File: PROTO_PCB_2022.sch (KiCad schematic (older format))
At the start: 38 parts, among them J1 12V_BATT, J10 12V_OUT_AUX, J11 SW_START, J12 VESC_START, J13 5V_OUT_AUX, J2 SW_KILL_DRIVER, J3 SW_KILL_LEFT, J4 SW_KILL_RIGHT, J5 ECU_POWER, J6 SW_BRAKE, J7 12V_OUT_HORN, J8 BRAKELIGHT_POWER, J9 12V_OUT_TEL, Q1 MOSFET_ECU, Q2 MOSFET_BRAKE_LIGHT, U1 LD1117S50TR_SOT223

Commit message: did some more layout work
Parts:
- removed F6, F7: 1A, Fuse:Fuseholder_Blade_Mini_Keystone_3568, symbol Device:Fuse
- removed J10: 12V_OUT_AUX, Connector_Molex:Molex_Micro-Fit_3.0_43650-0200_1x02_P3.00mm_Horizontal, symbol PROTO_PCB_2022-rescue:B2B-PH-K-S_LF__SN_-dk_Rectangular-Connectors-Headers-Male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
- removed J13: 5V_OUT_AUX, Connector_Molex:Molex_Micro-Fit_3.0_43650-0200_1x02_P3.00mm_Horizontal, symbol PROTO_PCB_2022-rescue:B2B-PH-K-S_LF__SN_-dk_Rectangular-Connectors-Headers-Male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
- J9: value 12V_OUT_TEL -> 12V_OUT_AUX
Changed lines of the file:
@@
 P 6200 1500
 F 0 "J9" V 6291 1372 50  0000 R CNN
-F 1 "12V_OUT_TEL" V 6200 1372 50  0000 R CNN
+F 1 "12V_OUT_AUX" V 6200 1372 50  0000 R CNN
 F 2 "Connector_Molex:Molex_Micro-Fit_3.0_43650-0200_1x02_P3.00mm_Horizontal" H 6400 1700 60  0001 L CNN
 F 3 "" H 6400 1800 60  0001 L CNN
@@
 	1    0    0    -1
 $EndComp
-$Comp
-L Device:Fuse F5
-U 1 1 62844314
-P 5800 1400
-F 0 "F5" V 5603 1400 50  0000 C CNN
-F 1 "1A" V 5694 1400 50  0000 C CNN
-F 2 "Fuse:Fuseholder_Blade_Mini_Keystone_3568" V 5730 1400 50  0001 C CNN
-F 3 "https://www.digikey.ca/en/products/detail/littelfuse-inc/178-6164-0001/2515818" H 5800 1400 50  0001 C CNN
-	1    5800 1400
-	0    1    1    0
-$EndComp
 Wire Wire Line
 	5500 1150 5500 1400
-Wire Wire Line
-	5500 1400 5650 1400
-Wire Wire Line
-	5950 1400 6100 1400
 $Comp
 L power:GND #PWR012
@@
 Wire Wire Line
 	5500 1500 5500 1700
-$Comp
-L PROTO_PCB_2022-rescue:B2B-PH-K-S_LF__SN_-dk_Rectangular-Connectors-Headers-Male-Pins-Proto-PCB's-combined-rescue-Proto-PCB's-combined-rescue J10
-U 1 1 6284D1CD
-P 7700 1500
-F 0 "J10" V 7791 1372 50  0000 R CNN
-F 1 "12V_OUT_AUX" V 7700 1372 50  0000 R CNN
-F 2 "Connector_Molex:Molex_Micro-Fit_3.0_43650-0200_1x02_P3.00mm_Horizontal" H 7900 1700 60  0001 L CNN
-F 3 "" H 7900 1800 60  0001 L CNN
-F 4 "" H 7900 1900 60  0001 L CNN "DigiKeyPN"
-F 5 "0436500201" H 7900 2000 60  0001 L CNN "MPN"
-	1    7700 1500
-	0    -1   -1   0
-$EndComp
-$Comp
-L power:+12V #PWR015
-U 1 1 6284D1D7
-P 7000 1150
-F 0 "#PWR015" H 7000 1000 50  0001 C CNN
-F 1 "+12V" H 7015 1323 50  0000 C CNN
-F 2 "" H 7000 1150 50  0001 C CNN
-F 3 "" H 7000 1150 50  0001 C CNN
-	1    7000 1150
-	1    0    0    -1
-$EndComp
-$Comp
-L Device:Fuse F6
-U 1 1 6284D1E1
-P 7300 1400
-F 0 "F6" V 7103 1400 50  0000 C CNN
-F 1 "1A" V 7194 1400 50  0000 C CNN
-F 2 "Fuse:Fuseholder_Blade_Mini_Keystone_3568" V 7230 1400 50  0001 C CNN
-F 3 "https://www.digikey.ca/en/products/detail/littelfuse-inc/178-6164-0001/2515818" H 7300 1400 50  0001 C CNN
-	1    7300 1400
-	0    1    1    0
-$EndComp
-Wire Wire Line
-	7000 1150 7000 1400
-Wire Wire Line
-	7000 1400 7150 1400
-Wire Wire Line
-	7450 1400 7600 1400
-$Comp
-L power:GND #PWR016
-U 1 1 6284D1EE
-P 7000 1700
-F 0 "#PWR016" H 7000 1450 50  0001 C CNN
-F 1 "GND" H 7005 1527 50  0000 C CNN
-F 2 "" H 7000 1700 50  0001 C CNN
-F 3 "" H 7000 1700 50  0001 C CNN
-	1    7000 1700
-	1    0    0    -1
-$EndComp
-Wire Wire Line
-	7600 1500 7000 1500
-Wire Wire Line
-	7000 1500 7000 1700
 $Comp
 L PROTO_PCB_2022-rescue:B2B-PH-K-S_LF__SN_-dk_Rectangular-Connectors-Headers-Male-Pins-Proto-PCB's-combined-rescue-Proto-PCB's-combined-rescue J2
@@
 Wire Wire Line
 	2650 3500 2650 3750
-$Comp
-L PROTO_PCB_2022-rescue:B2B-PH-K-S_LF__SN_-dk_Rectangular-Connectors-Headers-Male-Pins-Proto-PCB's-combined-rescue-Proto-PCB's-combined-rescue J13
-U 1 1 628AE5D5
-P 9250 1500
-F 0 "J13" V 9341 1372 50  0000 R CNN
-F 1 "5V_OUT_AUX" V 9250 1372 50  0000 R CNN
-F 2 "Connector_Molex:Molex_Micro-Fit_3.0_43650-0200_1x02_P3.00mm_Horizontal" H 9450 1700 60  0001 L CNN
-F 3 "" H 9450 1800 60  0001 L CNN
-F 4 "" H 9450 1900 60  0001 L CNN "DigiKeyPN"
-F 5 "0436500201" H 9450 2000 60  0001 L CNN "MPN"
-	1    9250 1500
-	0    -1   -1   0
-$EndComp
-$Comp
-L Device:Fuse F7
-U 1 1 628AE5E9
-P 8850 1400
-F 0 "F7" V 8653 1400 50  0000 C CNN
-F 1 "1A" V 8744 1400 50  0000 C CNN
-F 2 "Fuse:Fuseholder_Blade_Mini_Keystone_3568" V 8780 1400 50  0001 C CNN
-F 3 "https://www.digikey.ca/en/products/detail/littelfuse-inc/178-6164-0001/2515818" H 8850 1400 50  0001 C CNN
-	1    8850 1400
-	0    1    1    0
-$EndComp
-Wire Wire Line
-	8550 1150 8550 1400
-Wire Wire Line
-	8550 1400 8700 1400
-Wire Wire Line
-	9000 1400 9150 1400
-$Comp
-L power:GND #PWR020
-U 1 1 628AE5F6
-P 8550 1700
-F 0 "#PWR020" H 8550 1450 50  0001 C CNN
-F 1 "GND" H 8555 1527 50  0000 C CNN
-F 2 "" H 8550 1700 50  0001 C CNN
-F 3 "" H 8550 1700 50  0001 C CNN
-	1    8550 1700
-	1    0    0    -1
-$EndComp
-Wire Wire Line
-	9150 1500 8550 1500
-Wire Wire Line
-	8550 1500 8550 1700
 Wire Wire Line
 	3250 1500 3250 1650
 Wire Wire Line
 	2600 1950 2600 2050
-$Comp
-L power:+5V #PWR019
-U 1 1 628BB6ED
-P 8550 1150
-F 0 "#PWR019" H 8550 1000 50  0001 C CNN
-F 1 "+5V" H 8565 1323 50  0000 C CNN
-F 2 "" H 8550 1150 50  0001 C CNN
-F 3 "" H 8550 1150 50  0001 C CNN
-	1    8550 1150
-	1    0    0    -1
-$EndComp
 Wire Wire Line
 	5650 3650 5650 3750
@@
 Wire Wire Line
 	1100 1650 1100 1900
+$Comp
+L Device:Fuse F5
+U 1 1 627DA095
+P 5800 1400
+F 0 "F5" V 5603 1400 50  0000 C CNN
+F 1 "1A" V 5694 1400 50  0000 C CNN
+F 2 "Fuse:Fuseholder_Blade_Mini_Keystone_3568" V 5730 1400 50  0001 C CNN
+F 3 "https://www.digikey.ca/en/products/detail/littelfuse-inc/178-6164-0001/2515818" H 5800 1400 50  0001 C CNN
+	1    5800 1400
+	0    1    1    0
+$EndComp
+Wire Wire Line
+	5500 1400 5650 1400
+Wire Wire Line
+	5950 1400 6100 1400
 $EndSCHEMATC

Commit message: even more layout changes
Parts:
- removed F1: 10A, Fuse:Fuseholder_Blade_Mini_Keystone_3568, symbol Device:Fuse
- added D3: LED, LED_SMD:LED_1206_3216Metric, symbol Device:LED
- added R5: 1k, Resistor_SMD:R_1206_3216Metric, symbol Device:R
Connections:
- net +12V: now also J1.1
- net at J12.1: now also R5.2; no longer J11.2
- new net: D3.1 (K), R5.1
- new net: D3.2 (A), J11.2
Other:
- moved on the sheet: J11, J12
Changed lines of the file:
@@
 	1    0    0    -1
 $EndComp
-Connection ~ 2150 1650
 Wire Wire Line
 	2150 1950 2600 1950
@@
 L power:+12V #PWR02
 U 1 1 626F3385
-P 1800 1500
-F 0 "#PWR02" H 1800 1350 50  0001 C CNN
-F 1 "+12V" H 1815 1673 50  0000 C CNN
-F 2 "" H 1800 1500 50  0001 C CNN
-F 3 "" H 1800 1500 50  0001 C CNN
-	1    1800 1500
+P 1600 1500
+F 0 "#PWR02" H 1600 1350 50  0001 C CNN
+F 1 "+12V" H 1615 1673 50  0000 C CNN
+F 2 "" H 1600 1500 50  0001 C CNN
+F 3 "" H 1600 1500 50  0001 C CNN
+	1    1600 1500
 	1    0    0    -1
 $EndComp
@@
 	3050 1650 2900 1650
 $Comp
-L Device:Fuse F1
-U 1 1 62772F28
-P 1450 1650
-F 0 "F1" V 1253 1650 50  0000 C CNN
-F 1 "10A" V 1344 1650 50  0000 C CNN
-F 2 "Fuse:Fuseholder_Blade_Mini_Keystone_3568" V 1380 1650 50  0001 C CNN
-F 3 "https://www.digikey.ca/en/products/detail/littelfuse-inc/178-6164-0001/2515818" H 1450 1650 50  0001 C CNN
-	1    1450 1650
-	0    1    1    0
-$EndComp
-$Comp
 L power:PWR_FLAG #FLG01
 U 1 1 6266F354
-P 1800 1750
-F 0 "#FLG01" H 1800 1825 50  0001 C CNN
-F 1 "PWR_FLAG" H 1800 1923 50  0000 C CNN
-F 2 "" H 1800 1750 50  0001 C CNN
-F 3 "~" H 1800 1750 50  0001 C CNN
-	1    1800 1750
+P 1600 1750
+F 0 "#FLG01" H 1600 1825 50  0001 C CNN
+F 1 "PWR_FLAG" H 1600 1923 50  0000 C CNN
+F 2 "" H 1600 1750 50  0001 C CNN
+F 3 "~" H 1600 1750 50  0001 C CNN
+	1    1600 1750
 	-1   0    0    1
 $EndComp
@@
 	1200 1350 1200 1650
 Wire Wire Line
-	1200 1650 1300 1650
-Wire Wire Line
-	1800 1650 1800 1500
-Wire Wire Line
-	1800 1650 1800 1750
-Connection ~ 1800 1650
-Wire Wire Line
-	1600 1650 1800 1650
-Wire Wire Line
-	1800 1650 2150 1650
+	1600 1650 1600 1500
+Wire Wire Line
+	1600 1650 1600 1750
+Connection ~ 1600 1650
 Wire Wire Line
 	1100 1350 1100 1650
@@
 L PROTO_PCB_2022-rescue:B2B-PH-K-S_LF__SN_-dk_Rectangular-Connectors-Headers-Male-Pins-Proto-PCB's-combined-rescue-Proto-PCB's-combined-rescue J11
 U 1 1 628EA1D1
-P 7700 3250
-F 0 "J11" V 7791 3122 50  0000 R CNN
-F 1 "SW_START" V 7700 3122 50  0000 R CNN
-F 2 "Connector_Molex:Molex_Micro-Fit_3.0_43650-0200_1x02_P3.00mm_Horizontal" H 7900 3450 60  0001 L CNN
-F 3 "" H 7900 3550 60  0001 L CNN
-F 4 "" H 7900 3650 60  0001 L CNN "DigiKeyPN"
-F 5 "0436500201" H 7900 3750 60  0001 L CNN "MPN"
-	1    7700 3250
+P 7650 3500
+F 0 "J11" V 7741 3372 50  0000 R CNN
+F 1 "SW_START" V 7650 3372 50  0000 R CNN
+F 2 "Connector_Molex:Molex_Micro-Fit_3.0_43650-0200_1x02_P3.00mm_Horizontal" H 7850 3700 60  0001 L CNN
+F 3 "" H 7850 3800 60  0001 L CNN
+F 4 "" H 7850 3900 60  0001 L CNN "DigiKeyPN"
+F 5 "0436500201" H 7850 4000 60  0001 L CNN "MPN"
+	1    7650 3500
 	0    1    1    0
 $EndComp
-$Comp
-L PROTO_PCB_2022-rescue:B2B-PH-K-S_LF__SN_-dk_Rectangular-Connectors-Headers-Male-Pins-Proto-PCB's-combined-rescue-Proto-PCB's-combined-rescue J12
-U 1 1 628EA177
-P 8250 3350
-F 0 "J12" V 8341 3222 50  0000 R CNN
-F 1 "VESC_START" V 8250 3222 50  0000 R CNN
-F 2 "Connector_Molex:Molex_Micro-Fit_3.0_43650-0200_1x02_P3.00mm_Horizontal" H 8450 3550 60  0001 L CNN
-F 3 "" H 8450 3650 60  0001 L CNN
-F 4 "" H 8450 3750 60  0001 L CNN "DigiKeyPN"
-F 5 "0436500201" H 8450 3850 60  0001 L CNN "MPN"
-	1    8250 3350
-	0    -1   -1   0
-$EndComp
-Wire Wire Line
-	7800 3250 8150 3250
-Wire Wire Line
-	8150 3350 7800 3350
 $Comp
 L power:PWR_FLAG #FLG0101
@@
 Wire Wire Line
 	5950 1400 6100 1400
+$Comp
+L Device:R R5
+U 1 1 627D75F0
+P 8400 3700
+F 0 "R5" H 8470 3746 50  0000 L CNN
+F 1 "1k" H 8470 3655 50  0000 L CNN
+F 2 "Resistor_SMD:R_1206_3216Metric" V 8330 3700 50  0001 C CNN
+F 3 "~" H 8400 3700 50  0001 C CNN
+	1    8400 3700
+	0    -1   -1   0
+$EndComp
+$Comp
+L Device:LED D3
+U 1 1 627D75FA
+P 8000 3700
+F 0 "D3" V 8039 3582 50  0000 R CNN
+F 1 "LED" V 7948 3582 50  0000 R CNN
+F 2 "LED_SMD:LED_1206_3216Metric" H 8000 3700 50  0001 C CNN
+F 3 "https://www.digikey.ca/en/products/detail/lite-on-inc/LTST-C190KGKT/386815" H 8000 3700 50  0001 C CNN
+	1    8000 3700
+	-1   0    0    1
+$EndComp
+$Comp
+L PROTO_PCB_2022-rescue:B2B-PH-K-S_LF__SN_-dk_Rectangular-Connectors-Headers-Male-Pins-Proto-PCB's-combined-rescue-Proto-PCB's-combined-rescue J12
+U 1 1 628EA177
+P 8750 3600
+F 0 "J12" V 8841 3472 50  0000 R CNN
+F 1 "VESC_START" V 8750 3472 50  0000 R CNN
+F 2 "Connector_Molex:Molex_Micro-Fit_3.0_43650-0200_1x02_P3.00mm_Horizontal" H 8950 3800 60  0001 L CNN
+F 3 "" H 8950 3900 60  0001 L CNN
+F 4 "" H 8950 4000 60  0001 L CNN "DigiKeyPN"
+F 5 "0436500201" H 8950 4100 60  0001 L CNN "MPN"
+	1    8750 3600
+	0    -1   -1   0
+$EndComp
+Wire Wire Line
+	7750 3500 8650 3500
+Wire Wire Line
+	7750 3600 7750 3700
+Wire Wire Line
+	7750 3700 7850 3700
+Wire Wire Line
+	8150 3700 8250 3700
+Wire Wire Line
+	8550 3700 8650 3700
+Wire Wire Line
+	8650 3700 8650 3600
+Wire Wire Line
+	1200 1650 1600 1650
+Wire Wire Line
+	1600 1650 2150 1650
+Connection ~ 2150 1650
 $EndSCHEMATC

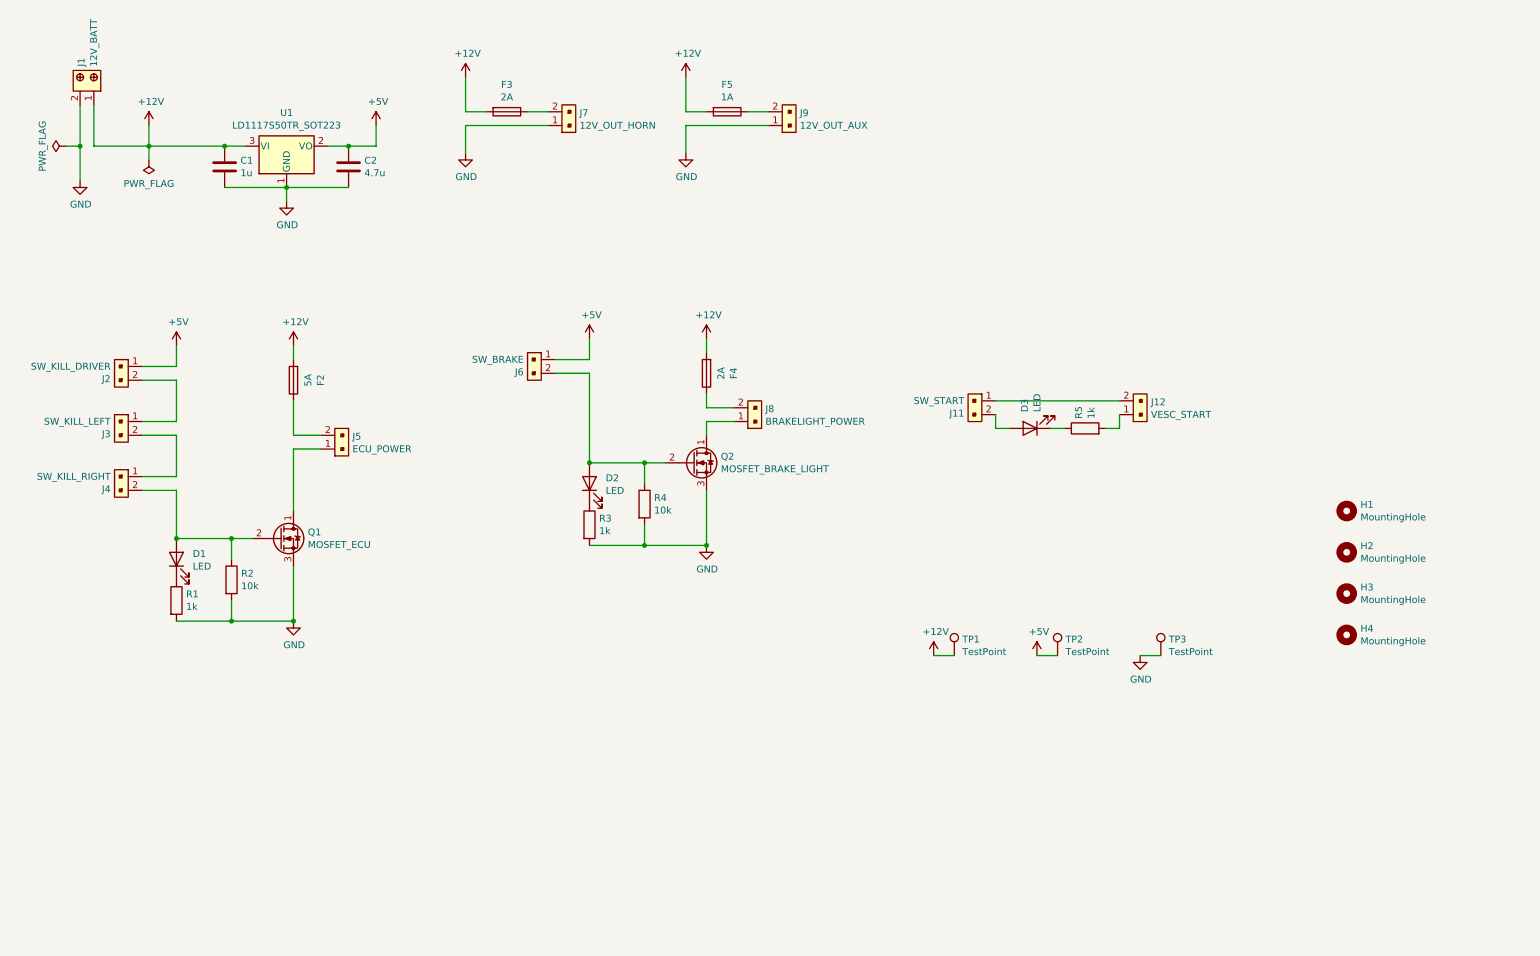
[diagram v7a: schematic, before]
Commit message: finishes schematic, footprint assignment, and BOM
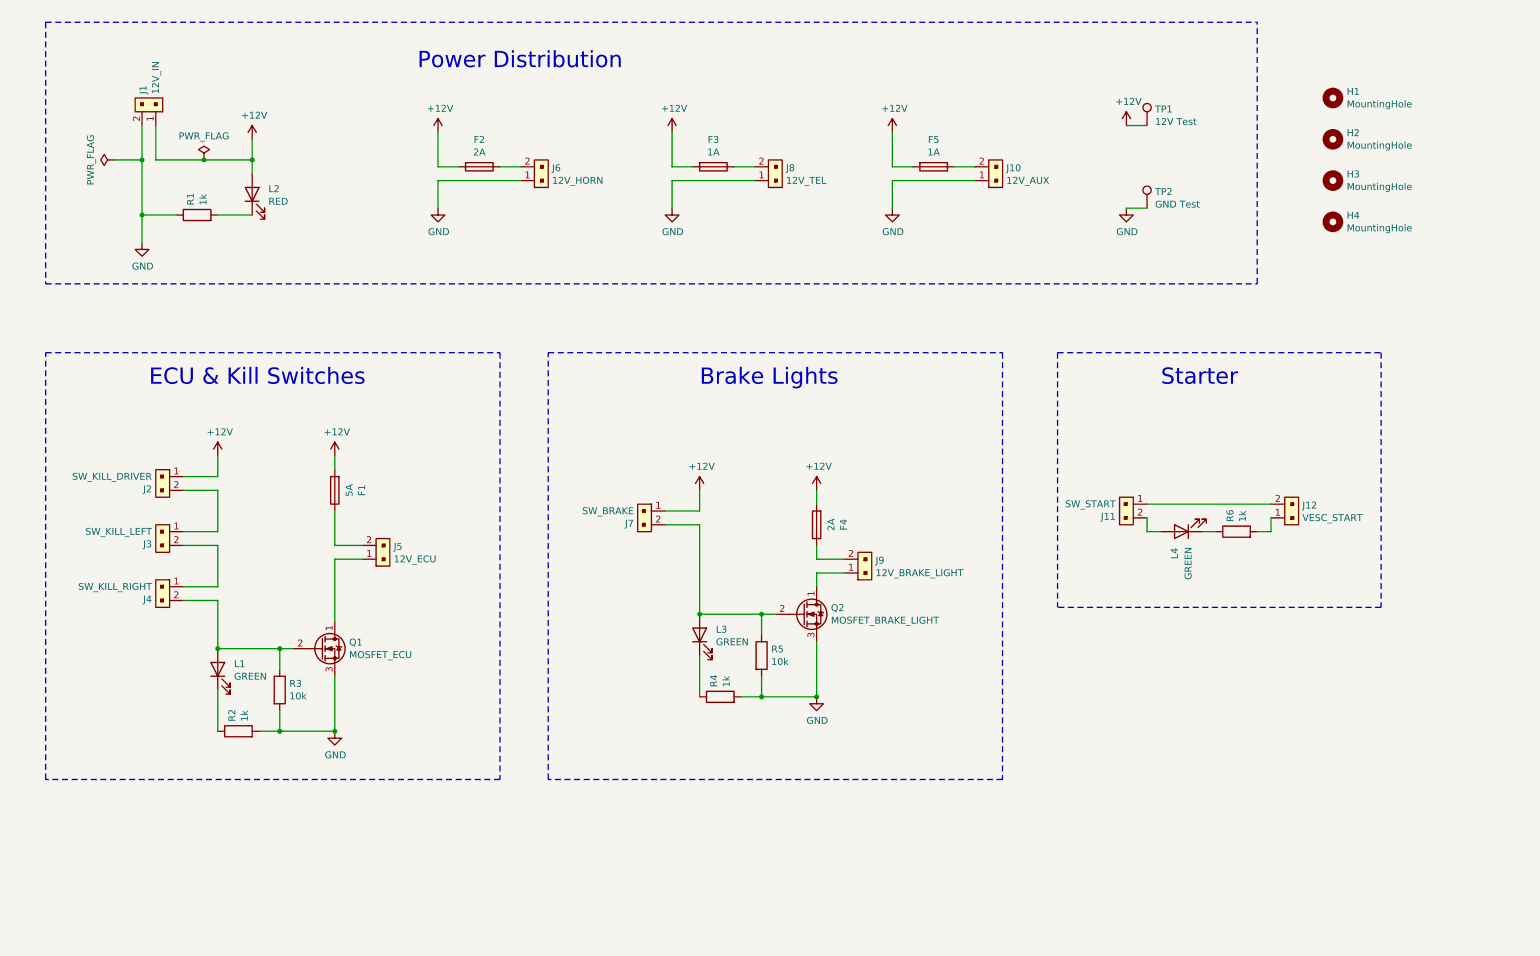
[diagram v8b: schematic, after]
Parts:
- removed C1: 1u, Capacitor_SMD:C_1206_3216Metric, symbol Device:C
- removed C2: 4.7u, Capacitor_SMD:C_1206_3216Metric, symbol Device:C
- removed J1: 12V_BATT, TerminalBlock_Phoenix:TerminalBlock_Phoenix_PT-1,5-2-5.0-H_1x02_P5.00mm_Horizontal, symbol PROTO_PCB_2022-rescue:1935161-dk_Terminal-Blocks-Wire-to-Board
- removed TP2: TestPoint, TestPoint:TestPoint_Keystone_5015_Micro-Minature, symbol Connector:TestPoint
- removed U1: LD1117S50TR_SOT223, Package_TO_SOT_SMD:SOT-223-3_TabPin2, symbol Regulator_Linear:LD1117S50TR_SOT223
- added F5: 1A, Fuse:Fuseholder_Blade_Mini_Keystone_3568, symbol Device:Fuse
- added J1: 12V_IN, Footprint Library:MOLEX_2002411212, symbol PROTO_PCB_2022-rescue:B2B-PH-K-S_LF__SN_-dk_Rectangular-Connectors-Headers-Male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
- added J10: 12V_AUX, Connector_Molex:Molex_Micro-Fit_3.0_43650-0200_1x02_P3.00mm_Horizontal, symbol PROTO_PCB_2022-rescue:B2B-PH-K-S_LF__SN_-dk_Rectangular-Connectors-Headers-Male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
- added L2: RED, LED_SMD:LED_1206_3216Metric, symbol Device:LED
- added R1: 1k, Resistor_SMD:R_1206_3216Metric, symbol Device:R
- J11, J12, J2, J3, J4: MPN 0436500201 -> (none)
- J5: value ECU_POWER -> 12V_ECU; MPN 0436500201 -> (none)
- J6: renamed from J7; value 12V_OUT_HORN -> 12V_HORN; MPN 0436500201 -> (none)
- J7: renamed from J6; MPN 0436500201 -> (none)
- J8: renamed from J9; value 12V_OUT_AUX -> 12V_TEL; MPN 0436500201 -> (none)
- J9: renamed from J8; value BRAKELIGHT_POWER -> 12V_BRAKE_LIGHT; MPN 0436500201 -> (none)
- L1: renamed from D1; value LED -> GREEN
- L3: renamed from D2; value LED -> GREEN
- L4: renamed from D3; value LED -> GREEN
- Q1, Q2: footprint Package_TO_SOT_SMD:SOT-23 -> Package_TO_SOT_SMD:TO-252-3_TabPin2; DigiKeyPN ZXMN3F30FHCT-ND -> (none); MPN ZXMN3F30FHTA -> (none)
- TP1: value TestPoint -> 12V Test
- TP2: renamed from TP3; value TestPoint -> GND Test
- renumbered F2 to F1, F3 to F2, F5 to F3, R1 to R2, R2 to R3, R3 to R4, R4 to R5, R5 to R6
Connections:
- net +5V is gone; now on net +12V: J2.1, J7.1
- net +12V: now also F5.2, J1.1, L2.2 (A)
- net GND: now also J1.2, J10.1, R1.1
- new net: F5.1, J10.2
- new net: L2.1 (K), R1.2
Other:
- note added: "Brake Lights"
- note added: "ECU & Kill Switches"
- note added: "Power Distribution"
- note added: "Starter"
- moved on the sheet: F1, F2, F3, F4, H1, H2, H3, H4, J11, J12, J2, J3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
